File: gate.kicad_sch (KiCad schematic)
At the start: 0 parts

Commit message: Added driver and powerstage
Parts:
- added C15, C17, C18, C21, C23, C24, C4, C6, C7: 100n, Capacitor_SMD:C_1206_3216Metric_Pad1.33x1.80mm_HandSolder, symbol Device:C
- added C16, C19, C20, C22, C25, C26, C5, C8, C9: 1u, Capacitor_SMD:C_1206_3216Metric_Pad1.33x1.80mm_HandSolder, symbol Device:C_Polarized_US
- added D1, D3, D4: D, Diode_SMD:D_SMA_Handsoldering, symbol Device:D
- added U4, U5, U6: IR2110, Package_DIP:DIP-14_W7.62mm_Socket_LongPads, symbol Driver_FET:IR2110
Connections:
- new net: C24.1, C26.1, D4.1 (K), U6.6 (VB)
- new net: C6.1, C8.1, D1.1 (K), U4.6 (VB)
- new net: C18.1, C20.1, D3.1 (K), U5.6 (VB)
- new net +12V: C15.1, C16.1, C17.1, C19.1, C21.1, C22.1, C23.1, C25.1, C4.1, C5.1, C7.1, C9.1, D1.2 (A), D3.2 (A), D4.2 (A), U4.3 (VCC), U4.9 (VDD), U5.3 (VCC), U5.9 (VDD), U6.3 (VCC), U6.9 (VDD)
- new net COM_A: C6.2, C8.2, U4.5 (VS)
- new net COM_B: C18.2, C20.2, U5.5 (VS)
- new net COM_C: C24.2, C26.2, U6.5 (VS)
- new net CTRL_AH: U4.10 (HIN)
- new net CTRL_AL: U4.12 (LIN)
- new net CTRL_BH: U5.10 (HIN)
- new net CTRL_BL: U5.12 (LIN)
- new net CTRL_CH: U6.10 (HIN)
- new net CTRL_CL: U6.12 (LIN)
- new net DRV_AH: U4.7 (HO)
- new net DRV_AL: U4.1 (LO)
- new net DRV_BH: U5.7 (HO)
- new net DRV_BL: U5.1 (LO)
- new net DRV_CH: U6.7 (HO)
- new net DRV_CL: U6.1 (LO)
- new net GND: C15.2, C16.2, C17.2, C19.2, C21.2, C22.2, C23.2, C25.2, C4.2, C5.2, C7.2, C9.2
- no-connect marks 0 -> 3
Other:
- note added: "BOOTSTRAP"

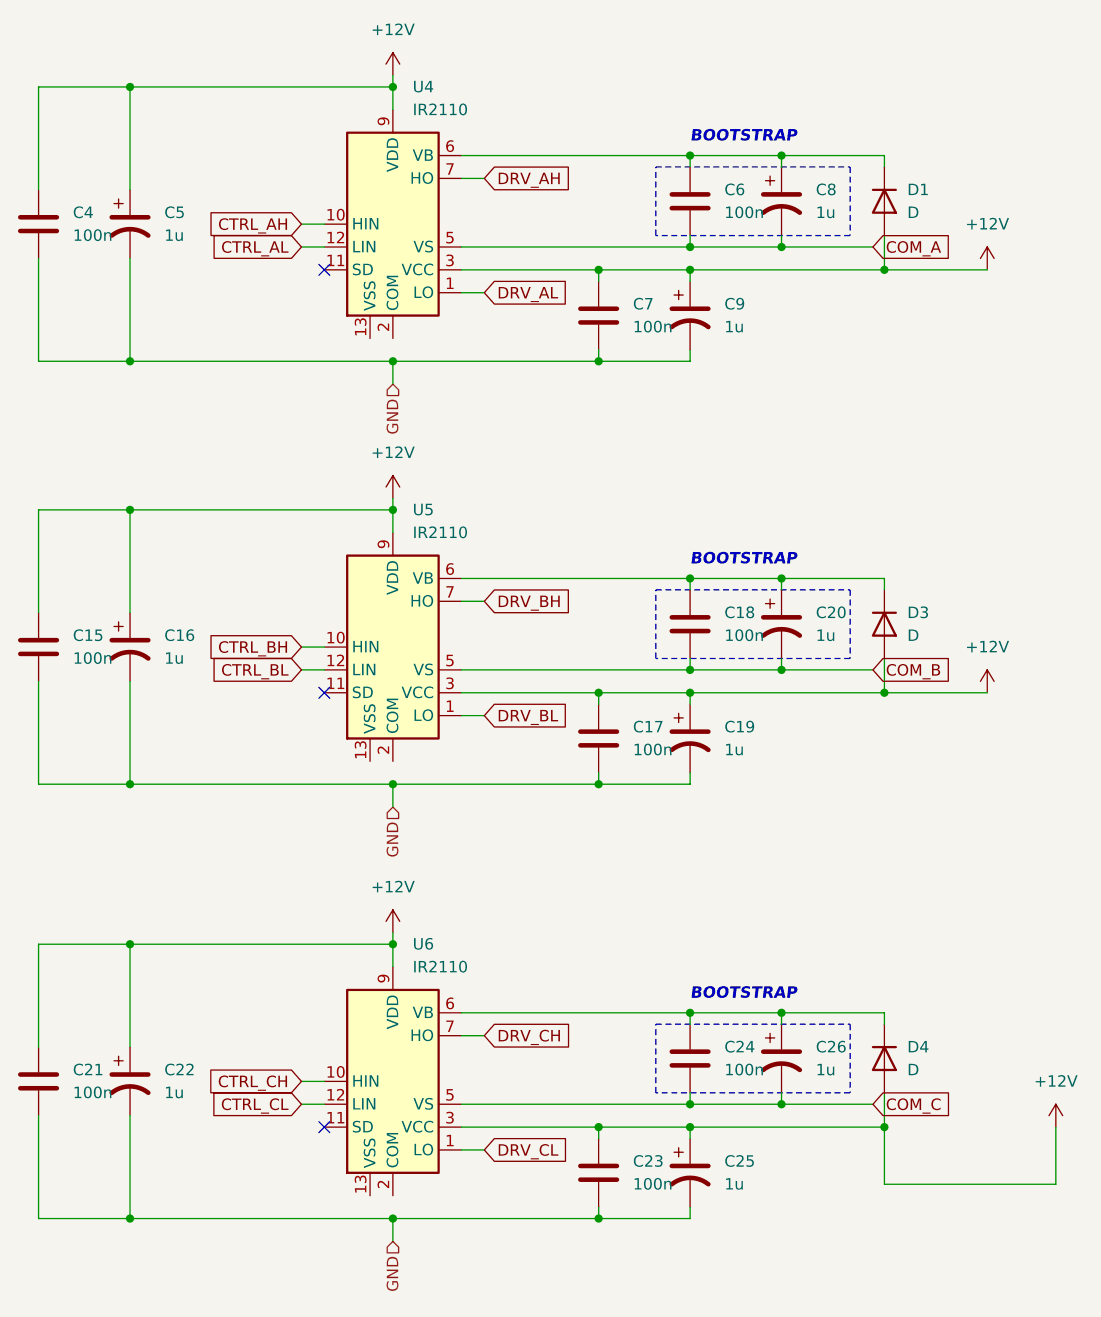
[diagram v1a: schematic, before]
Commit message: initial pcb placment, some components needs to be replaced by smd
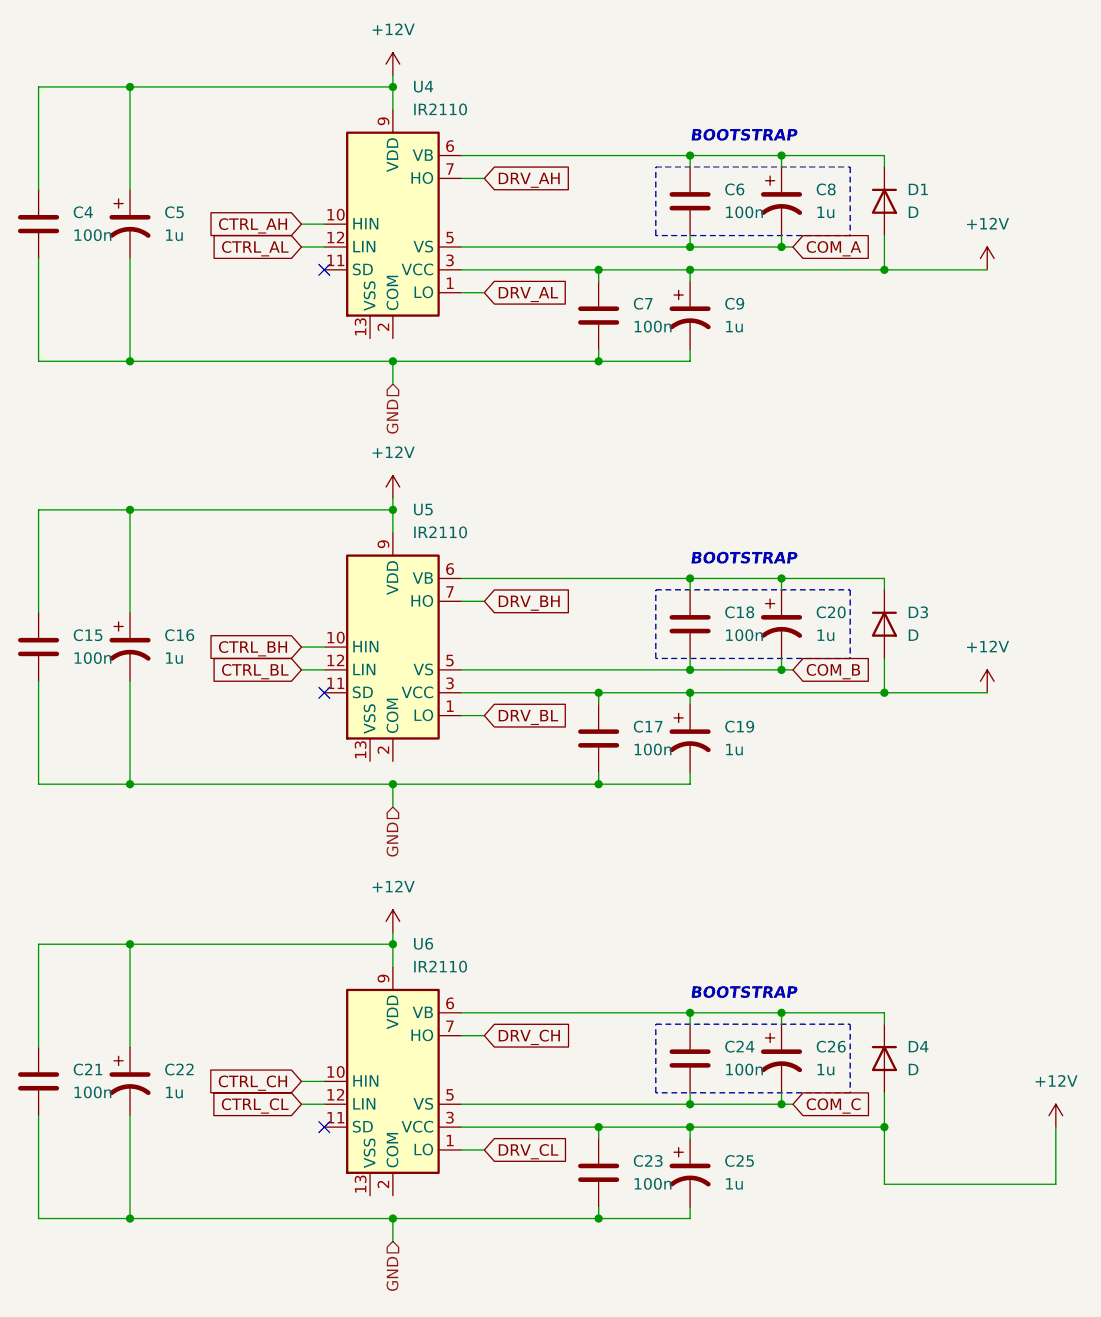
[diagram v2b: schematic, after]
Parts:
- C15, C16, C17, C18, C19, C20, C21, C22, C23, C24, C25, C26, C4, C5, C6, C7, C8, C9: footprint Capacitor_SMD:C_1206_3216Metric_Pad1.33x1.80mm_HandSolder -> Capacitor_THT:CP_Radial_Tantal_D5.5mm_P5.00mm
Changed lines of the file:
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@@
     (stroke (width 0) (type default))
   )
-  (wire (pts (xy 114.3 139.7) (xy 124.46 139.7))
+  (wire (pts (xy 114.3 139.7) (xy 115.57 139.7))
     (stroke (width 0) (type default))
   )
@@
     (stroke (width 0) (type default))
   )
-  (wire (pts (xy 114.3 44.45) (xy 124.46 44.45))
+  (wire (pts (xy 114.3 44.45) (xy 115.57 44.45))
     (stroke (width 0) (type default))
   )
@@
     (stroke (width 0) (type default))
   )
-  (wire (pts (xy 114.3 91.44) (xy 124.46 91.44))
+  (wire (pts (xy 114.3 91.44) (xy 115.57 91.44))
     (stroke (width 0) (type default))
   )
@@
     (effects (font (size 1.27 1.27) (thickness 0.254) bold italic) (justify left bottom))
   )
-  (global_label "COM_B" (shape input) (at 124.46 91.44 0) (fields_autoplaced)
+  (global_label "COM_B" (shape input) (at 115.57 91.44 0) (fields_autoplaced)
     (effects (font (size 1.27 1.27)) (justify left))
-    (property "Intersheetrefs" "${INTERSHEET_REFS}" (at 133.7347 91.44 0)
+    (property "Intersheetrefs" "${INTERSHEET_REFS}" (at 124.8447 91.44 0)
       (effects (font (size 1.27 1.27)) (justify left) hide)
     )
@@
     )
   )
-  (global_label "COM_A" (shape input) (at 124.46 44.45 0) (fields_autoplaced)
+  (global_label "COM_A" (shape input) (at 115.57 44.45 0) (fields_autoplaced)
     (effects (font (size 1.27 1.27)) (justify left))
-    (property "Intersheetrefs" "${INTERSHEET_REFS}" (at 133.5533 44.45 0)
+    (property "Intersheetrefs" "${INTERSHEET_REFS}" (at 124.6633 44.45 0)
       (effects (font (size 1.27 1.27)) (justify left) hide)
     )
@@
     )
   )
-  (global_label "COM_C" (shape input) (at 124.46 139.7 0) (fields_autoplaced)
+  (global_label "COM_C" (shape input) (at 115.57 139.7 0) (fields_autoplaced)
     (effects (font (size 1.27 1.27)) (justify left))
-    (property "Intersheetrefs" "${INTERSHEET_REFS}" (at 133.7347 139.7 0)
+    (property "Intersheetrefs" "${INTERSHEET_REFS}" (at 124.8447 139.7 0)
       (effects (font (size 1.27 1.27)) (justify left) hide)
     )
@@
       (effects (font (size 1.27 1.27)) (justify left))
     )
-    (property "Footprint" "Capacitor_SMD:C_1206_3216Metric_Pad1.33x1.80mm_HandSolder" (at 104.14 99.06 0)
+    (property "Footprint" "Capacitor_THT:CP_Radial_Tantal_D5.5mm_P5.00mm" (at 104.14 99.06 0)
       (effects (font (size 1.27 1.27)) hide)
     )
@@
       (effects (font (size 1.27 1.27)) (justify left))
     )
-    (property "Footprint" "Capacitor_SMD:C_1206_3216Metric_Pad1.33x1.80mm_HandSolder" (at 94.9452 151.13 0)
+    (property "Footprint" "Capacitor_THT:CP_Radial_Tantal_D5.5mm_P5.00mm" (at 94.9452 151.13 0)
       (effects (font (size 1.27 1.27)) hide)
     )
@@
       (effects (font (size 1.27 1.27)) (justify left))
     )
-    (property "Footprint" "Capacitor_SMD:C_1206_3216Metric_Pad1.33x1.80mm_HandSolder" (at 114.3 39.37 0)
+    (property "Footprint" "Capacitor_THT:CP_Radial_Tantal_D5.5mm_P5.00mm" (at 114.3 39.37 0)
       (effects (font (size 1.27 1.27)) hide)
     )
@@
       (effects (font (size 1.27 1.27)) (justify left))
     )
-    (property "Footprint" "Capacitor_SMD:C_1206_3216Metric_Pad1.33x1.80mm_HandSolder" (at 32.7152 45.72 0)
+    (property "Footprint" "Capacitor_THT:CP_Radial_Tantal_D5.5mm_P5.00mm" (at 32.7152 45.72 0)
       (effects (font (size 1.27 1.27)) hide)
     )
@@
       (effects (font (size 1.27 1.27)) (justify left))
     )
-    (property "Footprint" "Capacitor_SMD:C_1206_3216Metric_Pad1.33x1.80mm_HandSolder" (at 105.1052 43.18 0)
+    (property "Footprint" "Capacitor_THT:CP_Radial_Tantal_D5.5mm_P5.00mm" (at 105.1052 43.18 0)
       (effects (font (size 1.27 1.27)) hide)
     )
@@
       (effects (font (size 1.27 1.27)) (justify left))
     )
-    (property "Footprint" "Capacitor_SMD:C_1206_3216Metric_Pad1.33x1.80mm_HandSolder" (at 104.14 52.07 0)
+    (property "Footprint" "Capacitor_THT:CP_Radial_Tantal_D5.5mm_P5.00mm" (at 104.14 52.07 0)
       (effects (font (size 1.27 1.27)) hide)
     )
@@
       (effects (font (size 1.27 1.27)) (justify left))
     )
-    (property "Footprint" "Capacitor_SMD:C_1206_3216Metric_Pad1.33x1.80mm_HandSolder" (at 94.9452 102.87 0)
+    (property "Footprint" "Capacitor_THT:CP_Radial_Tantal_D5.5mm_P5.00mm" (at 94.9452 102.87 0)
       (effects (font (size 1.27 1.27)) hide)
     )
@@
       (effects (font (size 1.27 1.27)) (justify left))
     )
-    (property "Footprint" "Capacitor_SMD:C_1206_3216Metric_Pad1.33x1.80mm_HandSolder" (at 41.91 137.16 0)
+    (property "Footprint" "Capacitor_THT:CP_Radial_Tantal_D5.5mm_P5.00mm" (at 41.91 137.16 0)
       (effects (font (size 1.27 1.27)) hide)
     )
@@
       (effects (font (size 1.27 1.27)) (justify left))
     )
-    (property "Footprint" "Capacitor_SMD:C_1206_3216Metric_Pad1.33x1.80mm_HandSolder" (at 41.91 41.91 0)
+    (property "Footprint" "Capacitor_THT:CP_Radial_Tantal_D5.5mm_P5.00mm" (at 41.91 41.91 0)
       (effects (font (size 1.27 1.27)) hide)
     )
@@
       (effects (font (size 1.27 1.27)) (justify left))
     )
-    (property "Footprint" "Capacitor_SMD:C_1206_3216Metric_Pad1.33x1.80mm_HandSolder" (at 105.1052 90.17 0)
+    (property "Footprint" "Capacitor_THT:CP_Radial_Tantal_D5.5mm_P5.00mm" (at 105.1052 90.17 0)
       (effects (font (size 1.27 1.27)) hide)
     )
@@
       (effects (font (size 1.27 1.27)) (justify left))
     )
-    (property "Footprint" "Capacitor_SMD:C_1206_3216Metric_Pad1.33x1.80mm_HandSolder" (at 105.1052 138.43 0)
+    (property "Footprint" "Capacitor_THT:CP_Radial_Tantal_D5.5mm_P5.00mm" (at 105.1052 138.43 0)
       (effects (font (size 1.27 1.27)) hide)
     )
@@
       (effects (font (size 1.27 1.27)) (justify left))
     )
-    (property "Footprint" "Capacitor_SMD:C_1206_3216Metric_Pad1.33x1.80mm_HandSolder" (at 114.3 134.62 0)
+    (property "Footprint" "Capacitor_THT:CP_Radial_Tantal_D5.5mm_P5.00mm" (at 114.3 134.62 0)
       (effects (font (size 1.27 1.27)) hide)
     )
@@
       (effects (font (size 1.27 1.27)) (justify left))
     )
-    (property "Footprint" "Capacitor_SMD:C_1206_3216Metric_Pad1.33x1.80mm_HandSolder" (at 104.14 147.32 0)
+    (property "Footprint" "Capacitor_THT:CP_Radial_Tantal_D5.5mm_P5.00mm" (at 104.14 147.32 0)
       (effects (font (size 1.27 1.27)) hide)
     )
@@
       (effects (font (size 1.27 1.27)) (justify left))
     )
-    (property "Footprint" "Capacitor_SMD:C_1206_3216Metric_Pad1.33x1.80mm_HandSolder" (at 32.7152 92.71 0)
+    (property "Footprint" "Capacitor_THT:CP_Radial_Tantal_D5.5mm_P5.00mm" (at 32.7152 92.71 0)
       (effects (font (size 1.27 1.27)) hide)
     )
@@
       (effects (font (size 1.27 1.27)) (justify left))
     )
-    (property "Footprint" "Capacitor_SMD:C_1206_3216Metric_Pad1.33x1.80mm_HandSolder" (at 114.3 86.36 0)
+    (property "Footprint" "Capacitor_THT:CP_Radial_Tantal_D5.5mm_P5.00mm" (at 114.3 86.36 0)
       (effects (font (size 1.27 1.27)) hide)
     )
@@
       (effects (font (size 1.27 1.27)) (justify left))
     )
-    (property "Footprint" "Capacitor_SMD:C_1206_3216Metric_Pad1.33x1.80mm_HandSolder" (at 32.7152 140.97 0)
+    (property "Footprint" "Capacitor_THT:CP_Radial_Tantal_D5.5mm_P5.00mm" (at 32.7152 140.97 0)
       (effects (font (size 1.27 1.27)) hide)
     )
@@
       (effects (font (size 1.27 1.27)) (justify left))
     )
-    (property "Footprint" "Capacitor_SMD:C_1206_3216Metric_Pad1.33x1.80mm_HandSolder" (at 94.9452 55.88 0)
+    (property "Footprint" "Capacitor_THT:CP_Radial_Tantal_D5.5mm_P5.00mm" (at 94.9452 55.88 0)
       (effects (font (size 1.27 1.27)) hide)
     )
@@
       (effects (font (size 1.27 1.27)) (justify left))
     )
-    (property "Footprint" "Capacitor_SMD:C_1206_3216Metric_Pad1.33x1.80mm_HandSolder" (at 41.91 88.9 0)
-      (effects (font (size 1.27 1.27)) hide)
-    )
+    (property "Footprint" "Capacitor_THT:CP_Radial_Tantal_D5.5mm_P5.00mm" (at 41.91 88.9 0)
+      (effects (font (size 1.27 1.27)) hide)
+    )

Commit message: Added first pcb design
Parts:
- C15, C17, C18, C21, C23, C24, C4, C6, C7: footprint Capacitor_THT:CP_Radial_Tantal_D5.5mm_P5.00mm -> Capacitor_SMD:C_0805_2012Metric_Pad1.18x1.45mm_HandSolder
- C16, C19, C20, C22, C25, C26, C5, C8, C9: footprint Capacitor_THT:CP_Radial_Tantal_D5.5mm_P5.00mm -> Capacitor_SMD:CP_Elec_5x4.4
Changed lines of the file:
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@@
       (effects (font (size 1.27 1.27)) (justify left))
     )
-    (property "Footprint" "Capacitor_THT:CP_Radial_Tantal_D5.5mm_P5.00mm" (at 104.14 99.06 0)
+    (property "Footprint" "Capacitor_SMD:CP_Elec_5x4.4" (at 104.14 99.06 0)
       (effects (font (size 1.27 1.27)) hide)
     )
@@
       (effects (font (size 1.27 1.27)) (justify left))
     )
-    (property "Footprint" "Capacitor_THT:CP_Radial_Tantal_D5.5mm_P5.00mm" (at 94.9452 151.13 0)
+    (property "Footprint" "Capacitor_SMD:C_0805_2012Metric_Pad1.18x1.45mm_HandSolder" (at 94.9452 151.13 0)
       (effects (font (size 1.27 1.27)) hide)
     )
@@
       (effects (font (size 1.27 1.27)) (justify left))
     )
-    (property "Footprint" "Capacitor_THT:CP_Radial_Tantal_D5.5mm_P5.00mm" (at 114.3 39.37 0)
+    (property "Footprint" "Capacitor_SMD:CP_Elec_5x4.4" (at 114.3 39.37 0)
       (effects (font (size 1.27 1.27)) hide)
     )
@@
       (effects (font (size 1.27 1.27)) (justify left))
     )
-    (property "Footprint" "Capacitor_THT:CP_Radial_Tantal_D5.5mm_P5.00mm" (at 32.7152 45.72 0)
+    (property "Footprint" "Capacitor_SMD:C_0805_2012Metric_Pad1.18x1.45mm_HandSolder" (at 32.7152 45.72 0)
       (effects (font (size 1.27 1.27)) hide)
     )
@@
       (effects (font (size 1.27 1.27)) (justify left))
     )
-    (property "Footprint" "Capacitor_THT:CP_Radial_Tantal_D5.5mm_P5.00mm" (at 105.1052 43.18 0)
+    (property "Footprint" "Capacitor_SMD:C_0805_2012Metric_Pad1.18x1.45mm_HandSolder" (at 105.1052 43.18 0)
       (effects (font (size 1.27 1.27)) hide)
     )
@@
       (effects (font (size 1.27 1.27)) (justify left))
     )
-    (property "Footprint" "Capacitor_THT:CP_Radial_Tantal_D5.5mm_P5.00mm" (at 104.14 52.07 0)
+    (property "Footprint" "Capacitor_SMD:CP_Elec_5x4.4" (at 104.14 52.07 0)
       (effects (font (size 1.27 1.27)) hide)
     )
@@
       (effects (font (size 1.27 1.27)) (justify left))
     )
-    (property "Footprint" "Capacitor_THT:CP_Radial_Tantal_D5.5mm_P5.00mm" (at 94.9452 102.87 0)
+    (property "Footprint" "Capacitor_SMD:C_0805_2012Metric_Pad1.18x1.45mm_HandSolder" (at 94.9452 102.87 0)
       (effects (font (size 1.27 1.27)) hide)
     )
@@
       (effects (font (size 1.27 1.27)) (justify left))
     )
-    (property "Footprint" "Capacitor_THT:CP_Radial_Tantal_D5.5mm_P5.00mm" (at 41.91 137.16 0)
+    (property "Footprint" "Capacitor_SMD:CP_Elec_5x4.4" (at 41.91 137.16 0)
       (effects (font (size 1.27 1.27)) hide)
     )
@@
       (effects (font (size 1.27 1.27)) (justify left))
     )
-    (property "Footprint" "Capacitor_THT:CP_Radial_Tantal_D5.5mm_P5.00mm" (at 41.91 41.91 0)
+    (property "Footprint" "Capacitor_SMD:CP_Elec_5x4.4" (at 41.91 41.91 0)
       (effects (font (size 1.27 1.27)) hide)
     )
@@
       (effects (font (size 1.27 1.27)) (justify left))
     )
-    (property "Footprint" "Capacitor_THT:CP_Radial_Tantal_D5.5mm_P5.00mm" (at 105.1052 90.17 0)
+    (property "Footprint" "Capacitor_SMD:C_0805_2012Metric_Pad1.18x1.45mm_HandSolder" (at 105.1052 90.17 0)
       (effects (font (size 1.27 1.27)) hide)
     )
@@
       (effects (font (size 1.27 1.27)) (justify left))
     )
-    (property "Footprint" "Capacitor_THT:CP_Radial_Tantal_D5.5mm_P5.00mm" (at 105.1052 138.43 0)
+    (property "Footprint" "Capacitor_SMD:C_0805_2012Metric_Pad1.18x1.45mm_HandSolder" (at 105.1052 138.43 0)
       (effects (font (size 1.27 1.27)) hide)
     )
@@
       (effects (font (size 1.27 1.27)) (justify left))
     )
-    (property "Footprint" "Capacitor_THT:CP_Radial_Tantal_D5.5mm_P5.00mm" (at 114.3 134.62 0)
+    (property "Footprint" "Capacitor_SMD:CP_Elec_5x4.4" (at 114.3 134.62 0)
       (effects (font (size 1.27 1.27)) hide)
     )
@@
       (effects (font (size 1.27 1.27)) (justify left))
     )
-    (property "Footprint" "Capacitor_THT:CP_Radial_Tantal_D5.5mm_P5.00mm" (at 104.14 147.32 0)
+    (property "Footprint" "Capacitor_SMD:CP_Elec_5x4.4" (at 104.14 147.32 0)
       (effects (font (size 1.27 1.27)) hide)
     )
@@
       (effects (font (size 1.27 1.27)) (justify left))
     )
-    (property "Footprint" "Capacitor_THT:CP_Radial_Tantal_D5.5mm_P5.00mm" (at 32.7152 92.71 0)
+    (property "Footprint" "Capacitor_SMD:C_0805_2012Metric_Pad1.18x1.45mm_HandSolder" (at 32.7152 92.71 0)
       (effects (font (size 1.27 1.27)) hide)
     )
@@
       (effects (font (size 1.27 1.27)) (justify left))
     )
-    (property "Footprint" "Capacitor_THT:CP_Radial_Tantal_D5.5mm_P5.00mm" (at 114.3 86.36 0)
+    (property "Footprint" "Capacitor_SMD:CP_Elec_5x4.4" (at 114.3 86.36 0)
       (effects (font (size 1.27 1.27)) hide)
     )
@@
       (effects (font (size 1.27 1.27)) (justify left))
     )
-    (property "Footprint" "Capacitor_THT:CP_Radial_Tantal_D5.5mm_P5.00mm" (at 32.7152 140.97 0)
+    (property "Footprint" "Capacitor_SMD:C_0805_2012Metric_Pad1.18x1.45mm_HandSolder" (at 32.7152 140.97 0)
       (effects (font (size 1.27 1.27)) hide)
     )
@@
       (effects (font (size 1.27 1.27)) (justify left))
     )
-    (property "Footprint" "Capacitor_THT:CP_Radial_Tantal_D5.5mm_P5.00mm" (at 94.9452 55.88 0)
+    (property "Footprint" "Capacitor_SMD:C_0805_2012Metric_Pad1.18x1.45mm_HandSolder" (at 94.9452 55.88 0)
       (effects (font (size 1.27 1.27)) hide)
     )
@@
       (effects (font (size 1.27 1.27)) (justify left))
     )
-    (property "Footprint" "Capacitor_THT:CP_Radial_Tantal_D5.5mm_P5.00mm" (at 41.91 88.9 0)
-      (effects (font (size 1.27 1.27)) hide)
-    )
+    (property "Footprint" "Capacitor_SMD:CP_Elec_5x4.4" (at 41.91 88.9 0)
+      (effects (font (size 1.27 1.27)) hide)
+    )
